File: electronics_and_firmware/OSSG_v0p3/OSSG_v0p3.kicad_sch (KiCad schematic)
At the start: 61 parts, among them IC1 DW01A, J1 USB_B_Micro, Q1 FS8205A, Q2 Q_NPN_BEC, Q3 Q_NPN_BEC, SW1 SW_SPST, U1 ESP32-PICO-D4, U2 TP4056, U3 XC6222B331MRG, U4 FT232RQ

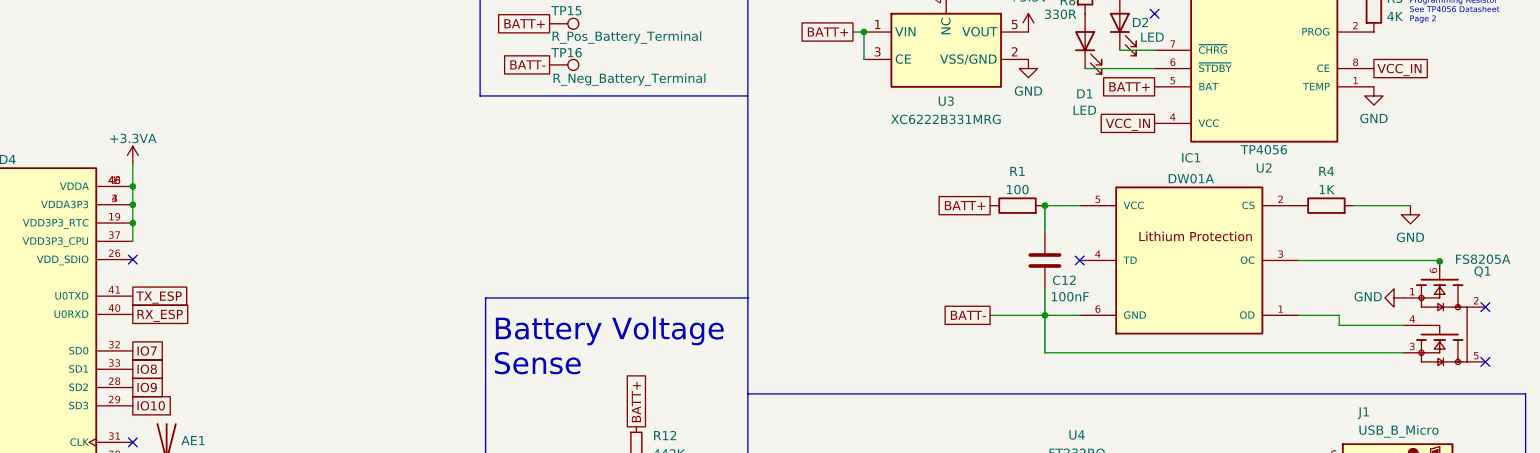
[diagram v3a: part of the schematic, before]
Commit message: more work on layout, small schematic fixes
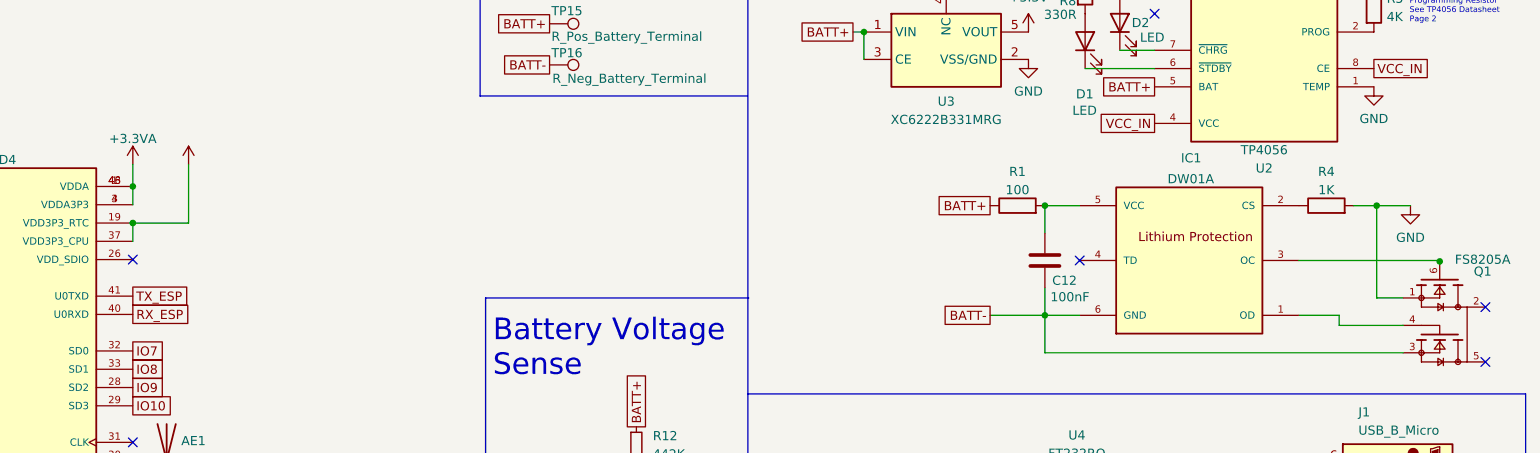
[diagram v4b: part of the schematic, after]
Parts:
- D1, D2: footprint (none) -> Diode_SMD:D_0402_1005Metric
- Q2, Q3: footprint (none) -> Package_TO_SOT_SMD:SOT-523
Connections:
- net +3.3VA: no longer U1.19 (VDD3P3_RTC), U1.37 (VDD3P3_CPU)
- net +3V3: now also U1.19 (VDD3P3_RTC), U1.37 (VDD3P3_CPU)

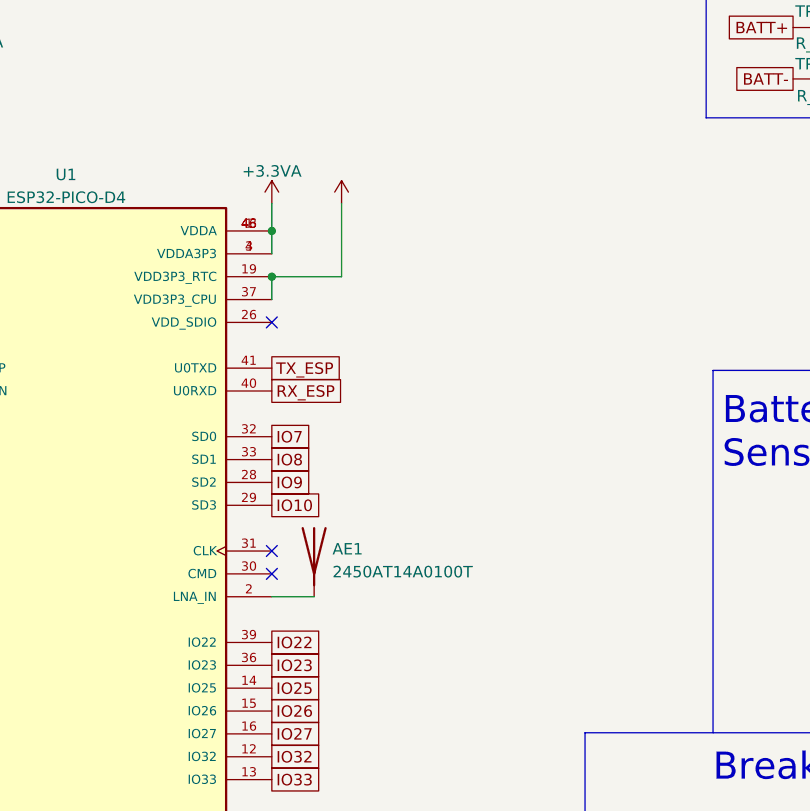
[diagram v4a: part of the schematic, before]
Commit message: Changed antenna and routing progress
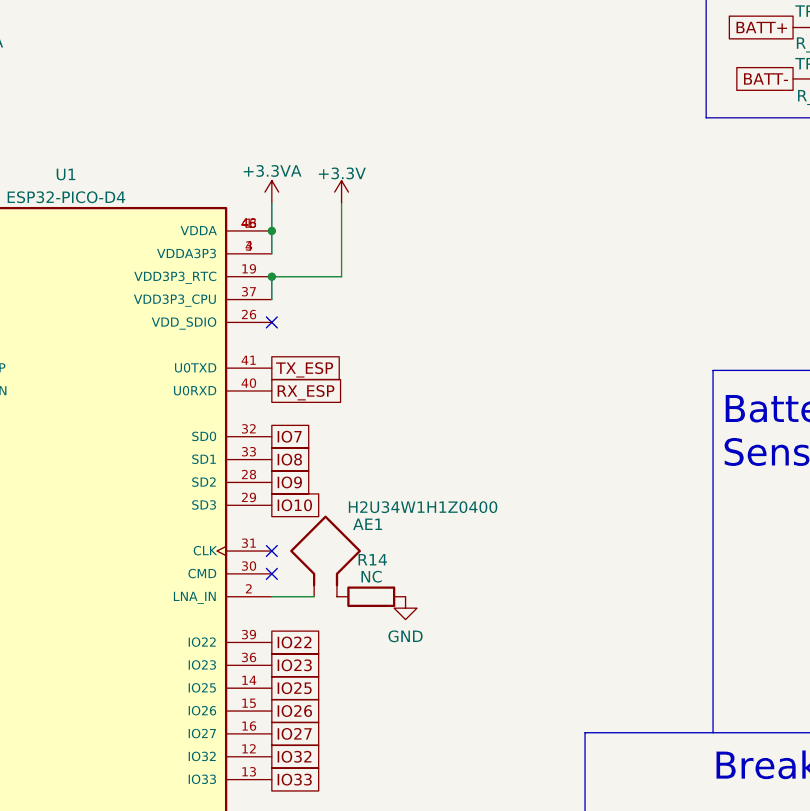
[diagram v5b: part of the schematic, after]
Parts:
- removed AE1: 2450AT14A0100T, Capacitor_SMD:C_0603_1608Metric, symbol Device:Antenna
- added AE1: H2U34W1H1Z0400, Resistor_SMD:R_1206_3216Metric, symbol Device:Antenna_Loop
- added R14: NC, Resistor_SMD:R_0402_1005Metric, symbol Device:R
- Q1: footprint Package_TO_SOT_SMD:SOT-23-6 -> ESPGLASSES:SOP65P640X120-8N
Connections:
- net GND: now also R14.2
- net at U1.2 (LNA_IN): now also AE1.1
- new net: AE1.2, R14.1
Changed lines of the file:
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@@
     (pin "2")
+  )
+  (symbol (lib_id "power:GND") (at 106.426 100.838 0) (unit 1)
+    (in_bom yes) (on_board yes) (fields_autoplaced)
+    (property "Reference" "#PWR0113" (id 0) (at 106.426 107.188 0)
+      (effects (font (size 1.27 1.27)) hide)
+    )
+    (property "Value" "GND" (id 1) (at 106.426 105.2814 0))
+    (property "Footprint" "" (id 2) (at 106.426 100.838 0)
+      (effects (font (size 1.27 1.27)) hide)
+    )
+    (property "Datasheet" "" (id 3) (at 106.426 100.838 0)
+      (effects (font (size 1.27 1.27)) hide)
+    )
+    (pin "1")
   )
   (symbol (lib_id "Connector:TestPoint") (at 162.052 131.318 90) (unit 1)
@@
     (pin "1")
   )
-  (symbol (lib_id "Device:Antenna") (at 96.266 95.758 0) (unit 1)
-    (in_bom yes) (on_board yes) (fields_autoplaced)
-    (property "Reference" "AE1" (id 0) (at 98.298 95.5583 0)
-      (effects (font (size 1.27 1.27)) (justify left))
-    )
-    (property "Value" "2450AT14A0100T" (id 1) (at 98.298 98.0952 0)
-      (effects (font (size 1.27 1.27)) (justify left))
-    )
-    (property "Footprint" "Capacitor_SMD:C_0603_1608Metric" (id 2) (at 96.266 95.758 0)
-      (effects (font (size 1.27 1.27)) hide)
-    )
-    (property "Datasheet" "~" (id 3) (at 96.266 95.758 0)
-      (effects (font (size 1.27 1.27)) hide)
-    )
-    (pin "1")
+  (symbol (lib_id "Device:R") (at 102.616 100.838 90) (unit 1)
+    (in_bom yes) (on_board yes)
+    (property "Reference" "R14" (id 0) (at 102.743 96.774 90))
+    (property "Value" "NC" (id 1) (at 102.616 98.6591 90))
+    (property "Footprint" "Resistor_SMD:R_0402_1005Metric" (id 2) (at 102.616 102.616 90)
+      (effects (font (size 1.27 1.27)) hide)
+    )
+    (property "Datasheet" "~" (id 3) (at 102.616 100.838 0)
+      (effects (font (size 1.27 1.27)) hide)
+    )
+    (pin "1")
+    (pin "2")
   )
   (symbol (lib_id "Connector:TestPoint") (at 162.052 138.557 90) (unit 1)
@@
     (pin "2")
   )
+  (symbol (lib_id "Device:Antenna_Loop") (at 96.266 95.758 0) (unit 1)
+    (in_bom yes) (on_board yes)
+    (property "Reference" "AE1" (id 0) (at 100.584 92.837 0)
+      (effects (font (size 1.27 1.27)) (justify left))
+    )
+    (property "Value" "H2U34W1H1Z0400" (id 1) (at 99.949 90.932 0)
+      (effects (font (size 1.27 1.27)) (justify left))
+    )
+    (property "Footprint" "Resistor_SMD:R_1206_3216Metric" (id 2) (at 96.266 95.758 0)
+      (effects (font (size 1.27 1.27)) hide)
+    )
+    (property "Datasheet" "~" (id 3) (at 96.266 95.758 0)
+      (effects (font (size 1.27 1.27)) hide)
+    )
+    (pin "1")
+    (pin "2")
+  )
   (symbol (lib_id "power:+3.3V") (at 99.314 57.15 0) (unit 1)
     (in_bom yes) (on_board yes)
@@
       (effects (font (size 1.27 1.27)) hide)
     )
-    (property "Value" "" (id 1) (at 99.314 53.848 0))
+    (property "Value" "+3.3V" (id 1) (at 99.314 53.848 0))
     (property "Footprint" "" (id 2) (at 99.314 57.15 0)
       (effects (font (size 1.27 1.27)) hide)
@@
     (property "Reference" "Q1" (id 0) (at 279.146 72.009 90))
     (property "Value" "FS8205A" (id 1) (at 279.146 70.358 90))
-    (property "Footprint" "Package_TO_SOT_SMD:SOT-23-6" (id 2) (at 260.477 84.582 0)
+    (property "Footprint" "ESPGLASSES:SOP65P640X120-8N" (id 2) (at 260.477 84.582 0)
       (effects (font (size 1.27 1.27)) (justify left bottom) hide)
     )
@@
       (reference "#PWR0112") (unit 1) (value "GND") (footprint "")
     )
-    (path "/3777412d-3741-4ca0-a315-3047d5599115"
-      (reference "AE1") (unit 1) (value "2450AT14A0100T") (footprint "Capacitor_SMD:C_0603_1608Metric")
+    (path "/200a58cb-92fe-4c06-b25f-32ea1d1203c1"
+      (reference "#PWR0113") (unit 1) (value "GND") (footprint "")
+    )
+    (path "/5509a4ed-a7b9-48bb-b455-fa2fff6d0c66"
+      (reference "AE1") (unit 1) (value "H2U34W1H1Z0400") (footprint "Resistor_SMD:R_1206_3216Metric")
     )
     (path "/f88b4835-e2ea-46c6-bb0c-93876903a6c2"
@@
     )
     (path "/a04de155-a9e4-4973-9637-f8df58013709"
-      (reference "Q1") (unit 1) (value "FS8205A") (footprint "Package_TO_SOT_SMD:SOT-23-6")
+      (reference "Q1") (unit 1) (value "FS8205A") (footprint "ESPGLASSES:SOP65P640X120-8N")
     )
     (path "/ed7a30fa-81b6-4388-af3e-481371a7ff8c"
@@
       (reference "R13") (unit 1) (value "160K") (footprint "Resistor_SMD:R_0402_1005Metric")
     )
+    (path "/35dee398-0c17-4451-88c4-009a8414f1d8"
+      (reference "R14") (unit 1) (value "NC") (footprint "Resistor_SMD:R_0402_1005Metric")
+    )
     (path "/92534179-acae-4912-baf5-95c7fd0a3d18"

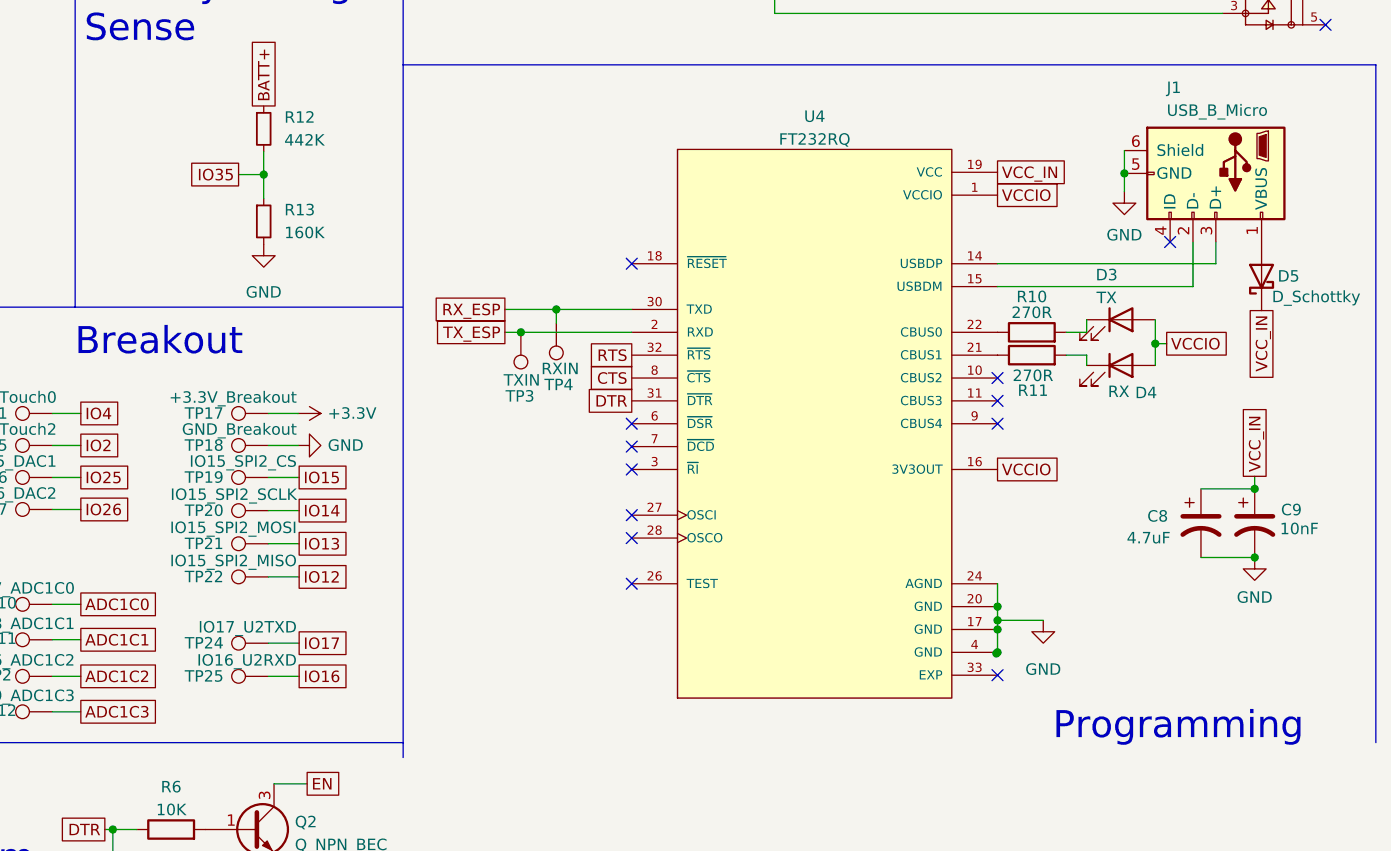
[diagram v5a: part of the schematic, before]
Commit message: lots of layout, fix footprint not found error, work towards better RF for antenna
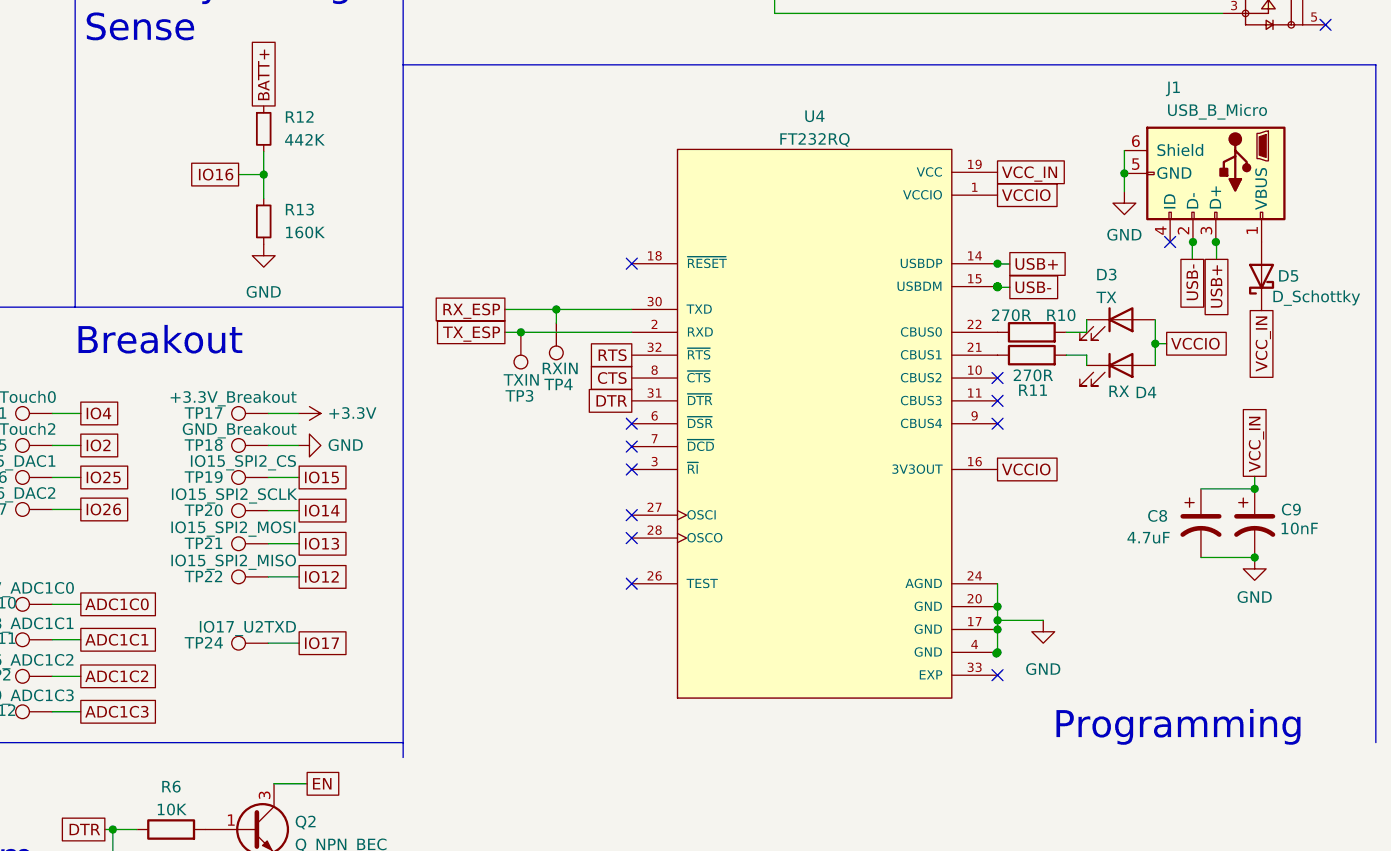
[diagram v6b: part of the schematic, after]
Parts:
- removed TP25: IO16_U2RXD, OpenSourceSmartGlasses:BreakoutPadSmall, symbol Connector:TestPoint
- Q1: footprint ESPGLASSES:SOP65P640X120-8N -> Package_TO_SOT_SMD:SOT-23-6
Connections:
- net IO16: now also R12.2, R13.1
- net IO35: no longer R12.2, R13.1
- net USB+: now reaches J1.3 (D+), U4.14 (USBDP)
- net USB-: now reaches J1.2 (D-), U4.15 (USBDM)

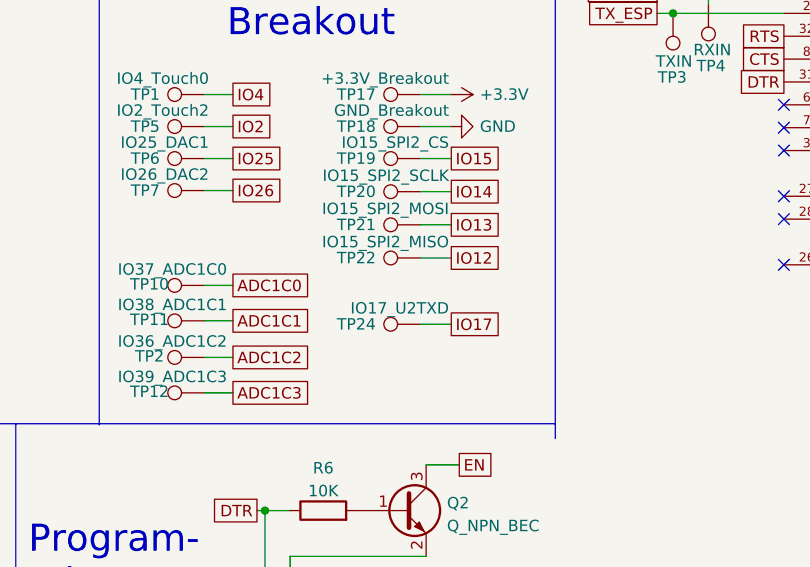
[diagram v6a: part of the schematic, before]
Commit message: change breakout test pads footprint size and start laying out breakouts
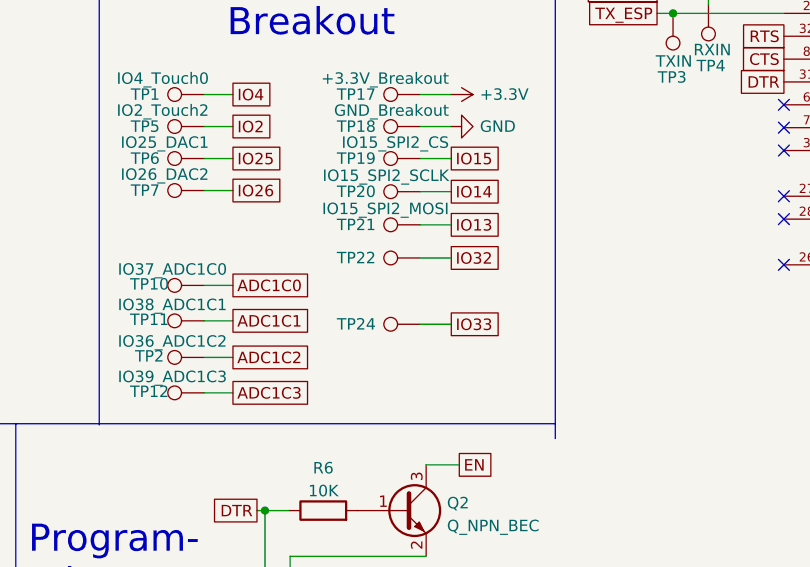
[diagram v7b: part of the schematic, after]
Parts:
- TP22: value IO15_SPI2_MISO -> (none)
- TP24: value IO17_U2TXD -> (none)
- TP3, TP4: footprint TestPoint:TestPoint_Pad_1.0x1.0mm -> TestPoint:TestPoint_Pad_D1.0mm
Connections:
- net IO12: no longer TP22.1
- net IO17: no longer TP24.1
- net IO32: now also TP22.1
- net IO33: now also TP24.1
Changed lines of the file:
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@@
     )
   )
-  (global_label "IO12" (shape passive) (at 165.481 145.923 0) (fields_autoplaced)
-    (effects (font (size 1.27 1.27)) (justify left))
-    (property "Intersheet References" "${INTERSHEET_REFS}" (id 0) (at 172.2484 146.0024 0)
+  (global_label "IO32" (shape passive) (at 165.481 145.923 0) (fields_autoplaced)
+    (effects (font (size 1.27 1.27)) (justify left))
+    (property "Intersheet References" "${INTERSHEET_REFS}" (id 0) (at 172.2484 145.8436 0)
       (effects (font (size 1.27 1.27)) (justify left) hide)
     )
@@
     )
   )
-  (global_label "IO17" (shape passive) (at 165.481 153.289 0) (fields_autoplaced)
-    (effects (font (size 1.27 1.27)) (justify left))
-    (property "Intersheet References" "${INTERSHEET_REFS}" (id 0) (at 172.2484 153.3684 0)
+  (global_label "IO33" (shape passive) (at 165.481 153.289 0) (fields_autoplaced)
+    (effects (font (size 1.27 1.27)) (justify left))
+    (property "Intersheet References" "${INTERSHEET_REFS}" (id 0) (at 172.2484 153.2096 0)
       (effects (font (size 1.27 1.27)) (justify left) hide)
     )
@@
       (effects (font (size 1.27 1.27)) (justify left))
     )
-    (property "Footprint" "TestPoint:TestPoint_Pad_1.0x1.0mm" (id 2) (at 185.039 118.745 0)
+    (property "Footprint" "TestPoint:TestPoint_Pad_D1.0mm" (id 2) (at 185.039 118.745 0)
       (effects (font (size 1.27 1.27)) hide)
     )
@@
       (effects (font (size 1.27 1.27)) (justify left))
     )
-    (property "Value" "IO15_SPI2_MISO" (id 1) (at 165.227 144.145 90)
+    (property "Value" "" (id 1) (at 165.227 144.145 90)
       (effects (font (size 1.27 1.27)) (justify left))
     )
@@
       (effects (font (size 1.27 1.27)) (justify left))
     )
-    (property "Value" "IO17_U2TXD" (id 1) (at 165.227 151.511 90)
+    (property "Value" "" (id 1) (at 165.227 151.511 90)
       (effects (font (size 1.27 1.27)) (justify left))
     )
@@
       (effects (font (size 1.27 1.27)) (justify left))
     )
-    (property "Footprint" "TestPoint:TestPoint_Pad_1.0x1.0mm" (id 2) (at 188.976 117.729 0)
+    (property "Footprint" "TestPoint:TestPoint_Pad_D1.0mm" (id 2) (at 188.976 117.729 0)
       (effects (font (size 1.27 1.27)) hide)
     )
@@
     )
     (path "/28efe4a8-0e69-4318-9ddb-738e50372ddb"
-      (reference "TP3") (unit 1) (value "TXIN") (footprint "TestPoint:TestPoint_Pad_1.0x1.0mm")
+      (reference "TP3") (unit 1) (value "TXIN") (footprint "TestPoint:TestPoint_Pad_D1.0mm")
     )
     (path "/e6a00c5e-0047-4e4a-a67c-295c3a134650"
-      (reference "TP4") (unit 1) (value "RXIN") (footprint "TestPoint:TestPoint_Pad_1.0x1.0mm")
+      (reference "TP4") (unit 1) (value "RXIN") (footprint "TestPoint:TestPoint_Pad_D1.0mm")
     )
     (path "/c4191593-387e-454b-9f7c-f5525b2240a8"
@@
     )
     (path "/79af0d47-4a1f-4064-a765-3362fec8a841"
-      (reference "TP22") (unit 1) (value "IO15_SPI2_MISO") (footprint "OpenSourceSmartGlasses:BreakoutPadSmall")
+      (reference "TP22") (unit 1) (value "IO23_BO") (footprint "OpenSourceSmartGlasses:BreakoutPadSmall")
     )
     (path "/c17e4cce-a010-4926-b2f1-1ff2a1e8c14f"
-      (reference "TP24") (unit 1) (value "IO17_U2TXD") (footprint "OpenSourceSmartGlasses:BreakoutPadSmall")
+      (reference "TP24") (unit 1) (value "IO33_BO") (footprint "OpenSourceSmartGlasses:BreakoutPadSmall")
     )
     (path "/b136d079-1922-4e2c-b5d7-49459d0477e3"
